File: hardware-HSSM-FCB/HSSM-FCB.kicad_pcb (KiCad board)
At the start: 2 copper layers, 13 x 12 mm, 2 parts

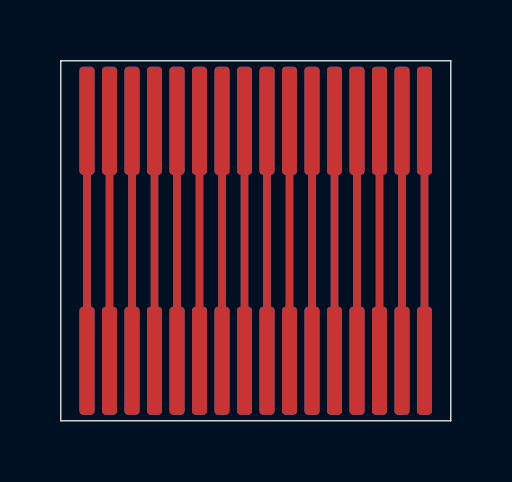
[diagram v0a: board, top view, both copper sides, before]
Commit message: [#11] Add vias for easier soldering and adjusted FCB size
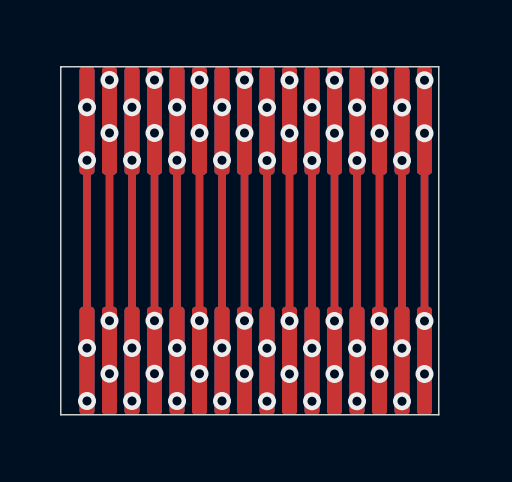
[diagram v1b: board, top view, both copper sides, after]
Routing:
- net Net-(CON1-Pad9): vias 0 -> 4
- net Net-(CON1-Pad8): vias 0 -> 4
- net Net-(CON1-Pad7): vias 0 -> 4
- net Net-(CON1-Pad6): vias 0 -> 4
- net Net-(CON1-Pad5): vias 0 -> 4
- net Net-(CON1-Pad4): vias 0 -> 4
- net Net-(CON1-Pad3): vias 0 -> 4
- net Net-(CON1-Pad2): vias 0 -> 4
- net Net-(CON1-Pad16): vias 0 -> 4
- net Net-(CON1-Pad15): vias 0 -> 4
- net Net-(CON1-Pad14): vias 0 -> 4
- net Net-(CON1-Pad13): vias 0 -> 4
- net Net-(CON1-Pad12): vias 0 -> 4
- net Net-(CON1-Pad11): vias 0 -> 4
- net Net-(CON1-Pad10): vias 0 -> 4
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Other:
- board size 13 x 12 mm -> 12.6 x 11.6 mm

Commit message: Fix outline, add board info and sn on silkscreen
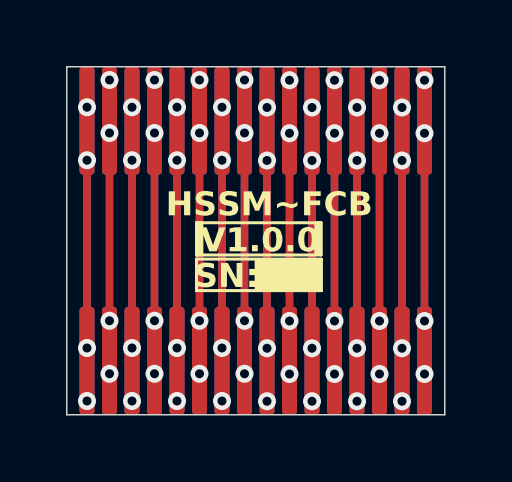
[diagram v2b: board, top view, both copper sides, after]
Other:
- board text added: "HSSM~FCB"
- board text added: "SN:"
- board text added: "V1.0.0"
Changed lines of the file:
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@@
 	)
 	(gr_rect
-		(start 117 130.2)
-		(end 129.6 141.8)
+		(start 123.5125 136.6625)
+		(end 125.6125 137.6375)
+		(stroke
+			(width 0.1)
+			(type solid)
+		)
+		(fill solid)
+		(layer "F.SilkS")
+	)
+	(gr_rect
+		(start 121.525 136.6125)
+		(end 125.6875 137.6625)
+		(stroke
+			(width 0.1)
+			(type default)
+		)
+		(fill none)
+		(layer "F.SilkS")
+	)
+	(gr_rect
+		(start 121.525 135.4)
+		(end 121.7 136.475)
+		(stroke
+			(width 0.1)
+			(type solid)
+		)
+		(fill solid)
+		(layer "F.SilkS")
+	)
+	(gr_rect
+		(start 125.5 135.4)
+		(end 125.675 136.45)
+		(stroke
+			(width 0.1)
+			(type solid)
+		)
+		(fill solid)
+		(layer "F.SilkS")
+	)
+	(gr_rect
+		(start 121.525 135.4)
+		(end 125.675 136.475)
+		(stroke
+			(width 0.1)
+			(type default)
+		)
+		(fill none)
+		(layer "F.SilkS")
+	)
+	(gr_rect
+		(start 117.2 130.2)
+		(end 129.8 141.8)
 		(stroke
 			(width 0.05)
@@
 		(layer "Edge.Cuts")
 	)
+	(gr_text "SN:"
+		(at 121.45 137.6375 0)
+		(layer "F.SilkS" knockout)
+		(effects
+			(font
+				(size 0.8 0.8)
+				(thickness 0.15)
+				(bold yes)
+			)
+			(justify left bottom)
+		)
+	)
+	(gr_text "HSSM~FCB"
+		(at 120.5 135.25 0)
+		(layer "F.SilkS" knockout)
+		(effects
+			(font
+				(size 0.8 0.8)
+				(thickness 0.15)
+				(bold yes)
+			)
+			(justify left bottom)
+		)
+	)
+	(gr_text "V1.0.0"
+		(at 121.65 136.45 0)
+		(layer "F.SilkS" knockout)
+		(effects
+			(font
+				(size 0.8 0.8)
+				(thickness 0.15)
+				(bold yes)
+			)
+			(justify left bottom)
+		)
+	)
 	(segment
